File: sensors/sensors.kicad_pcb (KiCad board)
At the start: 2 copper layers, 75 x 56 mm, 29 parts, among them J1 GPIO, J2 PWM, J3 Conn_01x16, J5 JP_GPS, J6 JP_RADIO, U1 SC16IS752IPW, Y1 14.7456MHz

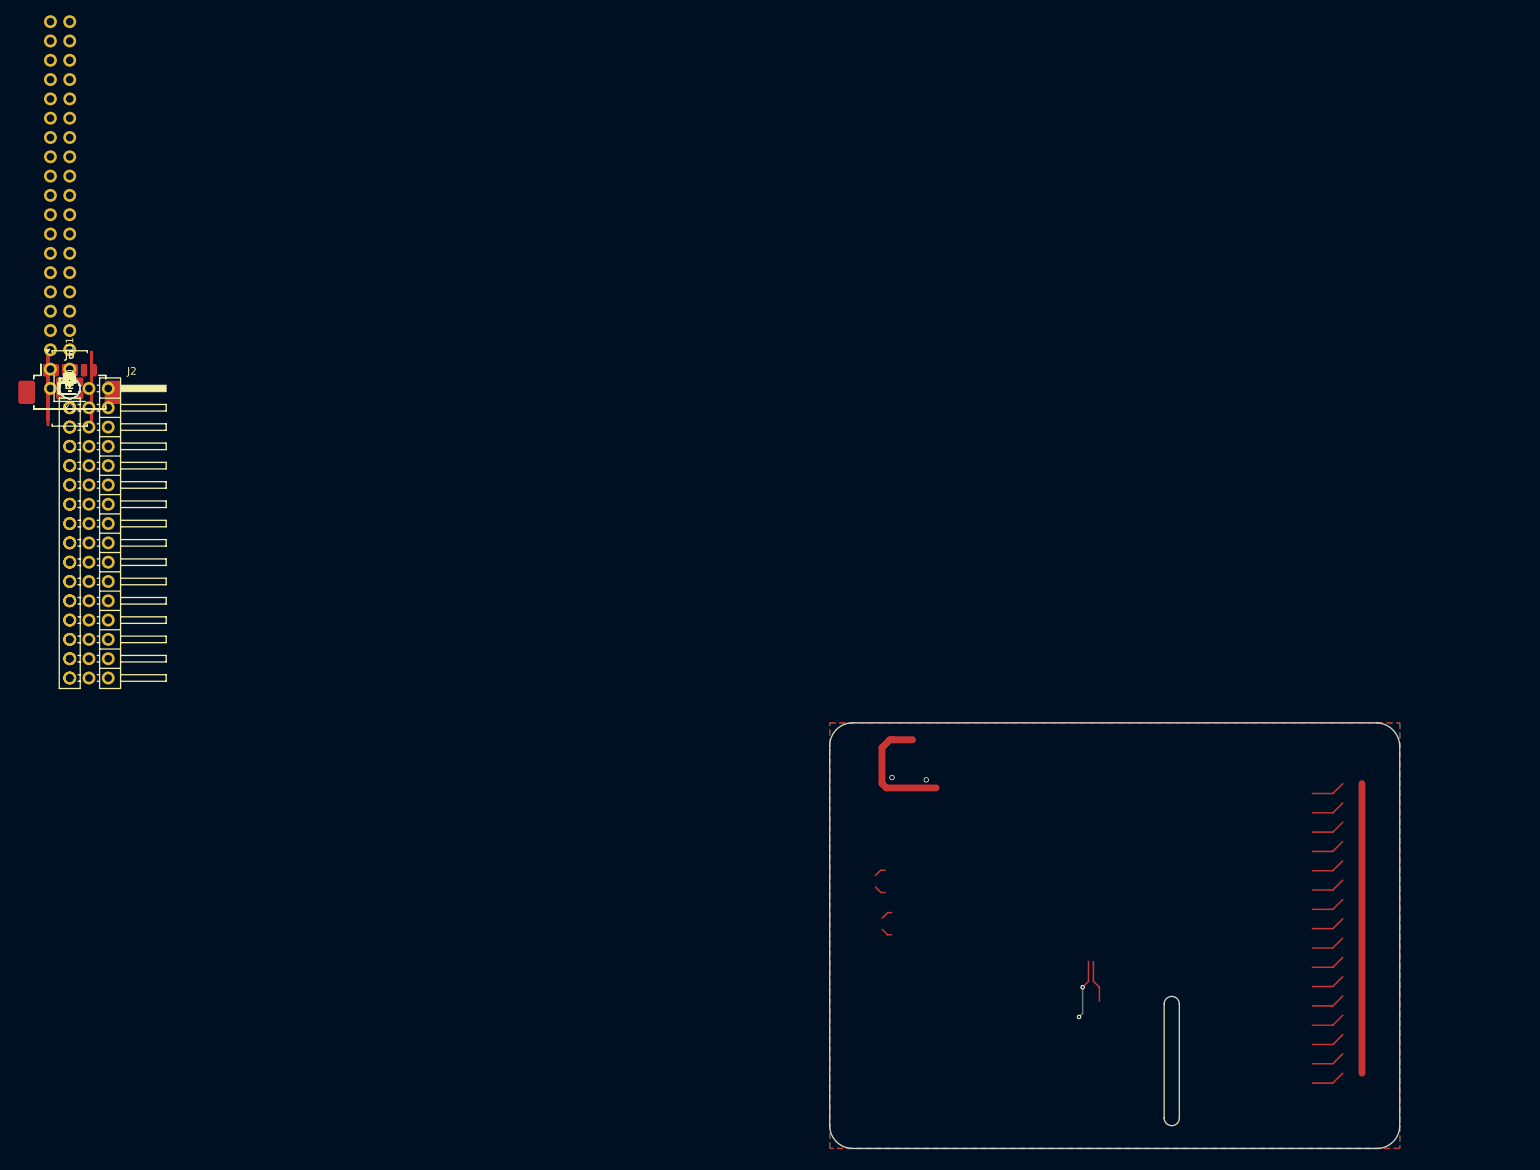
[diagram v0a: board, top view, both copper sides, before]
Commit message: add IMU
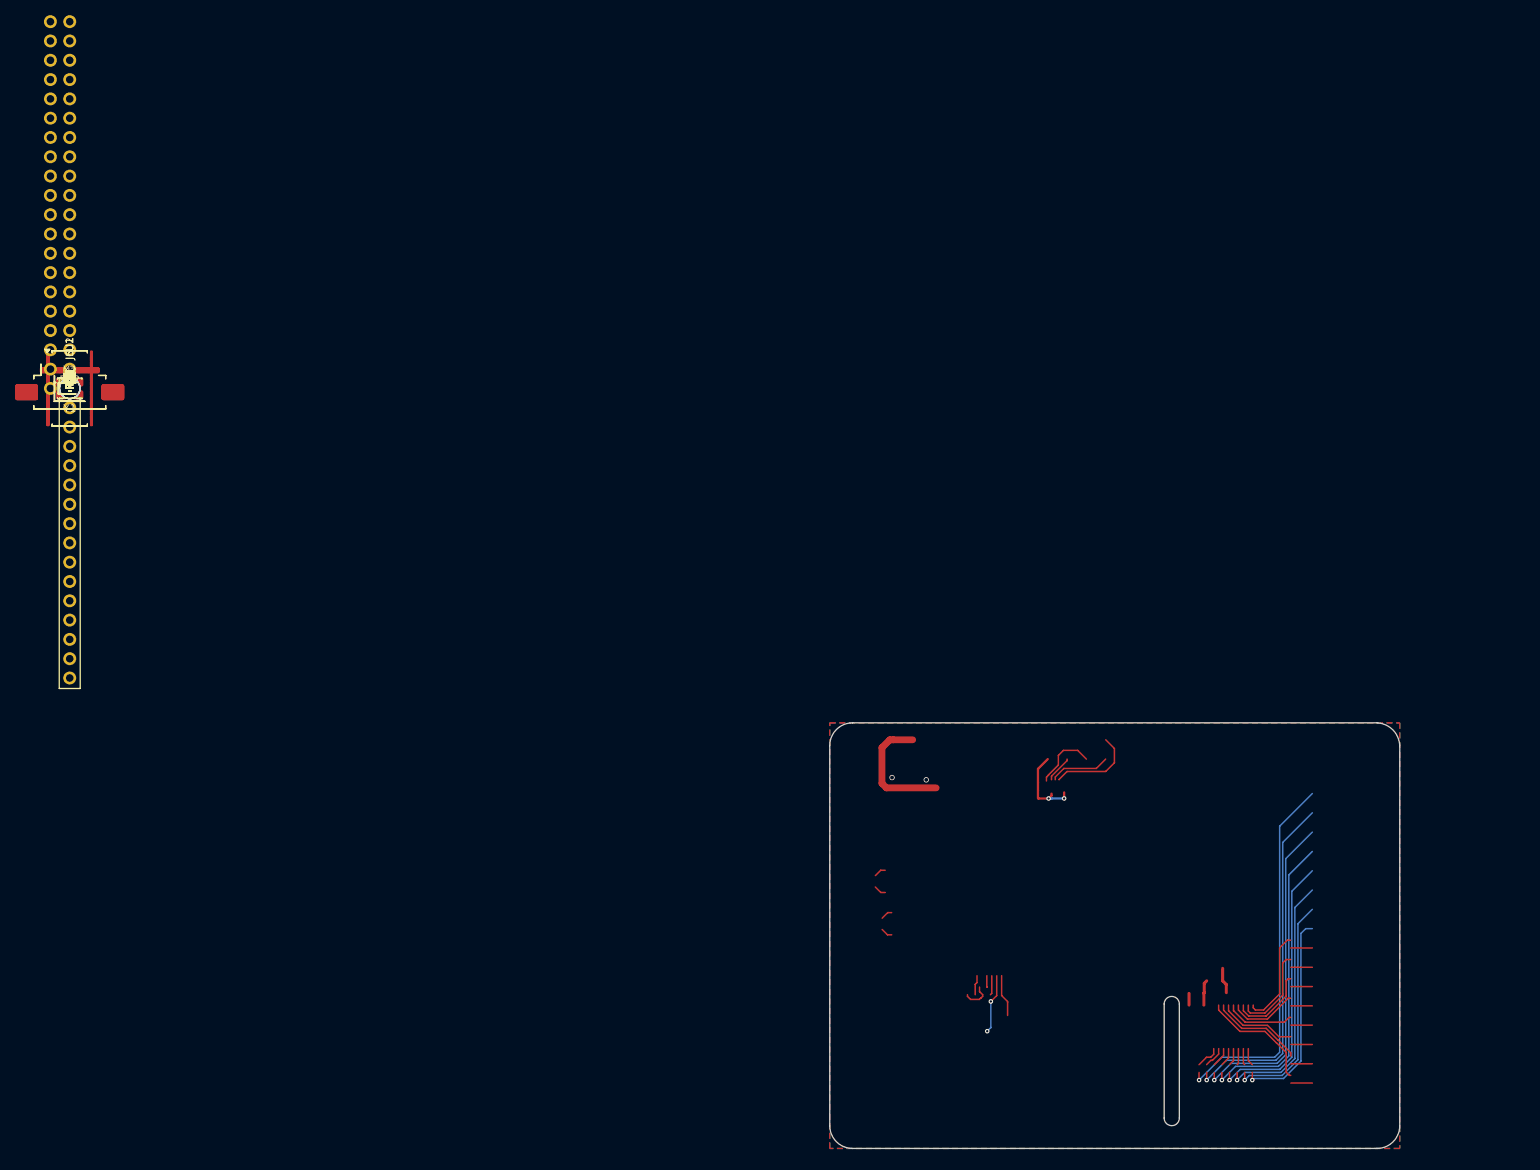
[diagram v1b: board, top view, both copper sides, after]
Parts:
- removed J2: PWM, pilotpi:PinHeader_3x16_P2.54mm_Horizontal
- added C4, C5, C6: 100nF (104) 10% 16V, Capacitor_SMD:C_0402_1005Metric, F.Cu at (0.00, 0.00)
- added C7: 220nF (224) 10% 16V, Capacitor_SMD:C_0402_1005Metric, F.Cu at (0.00, 0.00)
- added C8: 10nF (103) 10% 50V, Capacitor_SMD:C_0402_1005Metric, F.Cu at (0.00, 0.00)
- added R12: 3.3KΩ (3301) ±1%, Resistor_SMD:R_0402_1005Metric, F.Cu at (0.00, 0.00)
- added R13, R14, R15, R16, R17, R18, R19, R20, R21, R22, R23, R24, R25, R26, R27, R28: 220Ω (2200) ±1%, Resistor_SMD:R_0402_1005Metric, F.Cu at (0.00, 0.00)
- added U2: PCA9685PW, Package_SO:TSSOP-28_4.4x9.7mm_P0.65mm, F.Cu at (0.00, 0.00)
- added U3: ICM-42605, Package_LGA:LGA-14_3x2.5mm_P0.5mm_LayoutBorder3x4y, F.Cu at (0.00, 0.00)
- added Y2: ASE-xxxMHz, Oscillator:Oscillator_SMD_Abracon_ASE-4Pin_3.2x2.5mm, F.Cu at (0.00, 0.00)
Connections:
- J3 pad 1: /PWM15 -> /PWM0
- J3 pad 10: /PWM6 -> /PWM9
- J3 pad 11: /PWM5 -> /PWM10
- J3 pad 12: /PWM4 -> /PWM11
- J3 pad 13: /PWM3 -> /PWM12
- J3 pad 14: /PWM2 -> /PWM13
- J3 pad 15: /PWM1 -> /PWM14
- J3 pad 16: /PWM0 -> /PWM15
- J3 pad 2: /PWM14 -> /PWM1
- J3 pad 3: /PWM13 -> /PWM2
- J3 pad 4: /PWM12 -> /PWM3
- J3 pad 5: /PWM11 -> /PWM4
- J3 pad 6: /PWM10 -> /PWM5
- J3 pad 7: /PWM9 -> /PWM6
- J3 pad 8: /PWM8 -> /PWM7
- J3 pad 9: /PWM7 -> /PWM8
- J5 pad 4: unconnected-(J5-Pin_4-Pad4) -> /UART/CTSA
- J5 pad 5: unconnected-(J5-Pin_5-Pad5) -> /UART/RTSA
- R4 pad 1: GND -> +3V3
- R4 pad 2: Net-(U1-~{CTSA}) -> /UART/CTSA
- U1 pad 1: unconnected-(U1-~{RTSA}-Pad1) -> /UART/RTSA
- U1 pad 2: Net-(U1-~{CTSA}) -> /UART/CTSA
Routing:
- net /PWM0: track 4.54 -> 48.9 mm, vias 0 -> 1
- net /PWM1: track 4.54 -> 45.7 mm, vias 0 -> 1
- net /VCC_PWM: track 38.1 -> 0.00 mm
- net /PWM2: track 4.54 -> 42.5 mm, vias 0 -> 1
- net /PWM3: track 4.54 -> 39.3 mm, vias 0 -> 1
- net /PWM4: track 4.54 -> 36.1 mm, vias 0 -> 1
- net /PWM5: track 4.54 -> 32.9 mm, vias 0 -> 1
- net /PWM6: track 4.54 -> 29.7 mm, vias 0 -> 1
- net /PWM7: track 4.54 -> 27.0 mm, vias 0 -> 1
- net +3V3: track 0.00 -> 18.1 mm, vias 0 -> 2
- net Net-(U2-LED15): track 0.00 -> 15.2 mm
- net Net-(U2-LED8): track 0.00 -> 12.8 mm
- net Net-(U2-LED14): track 0.00 -> 12.3 mm
- net Net-(U2-LED9): track 0.00 -> 11.9 mm
- net /GPIO8/SPI0.CE0: track 0.00 -> 11.7 mm
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
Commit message: add magnetometer
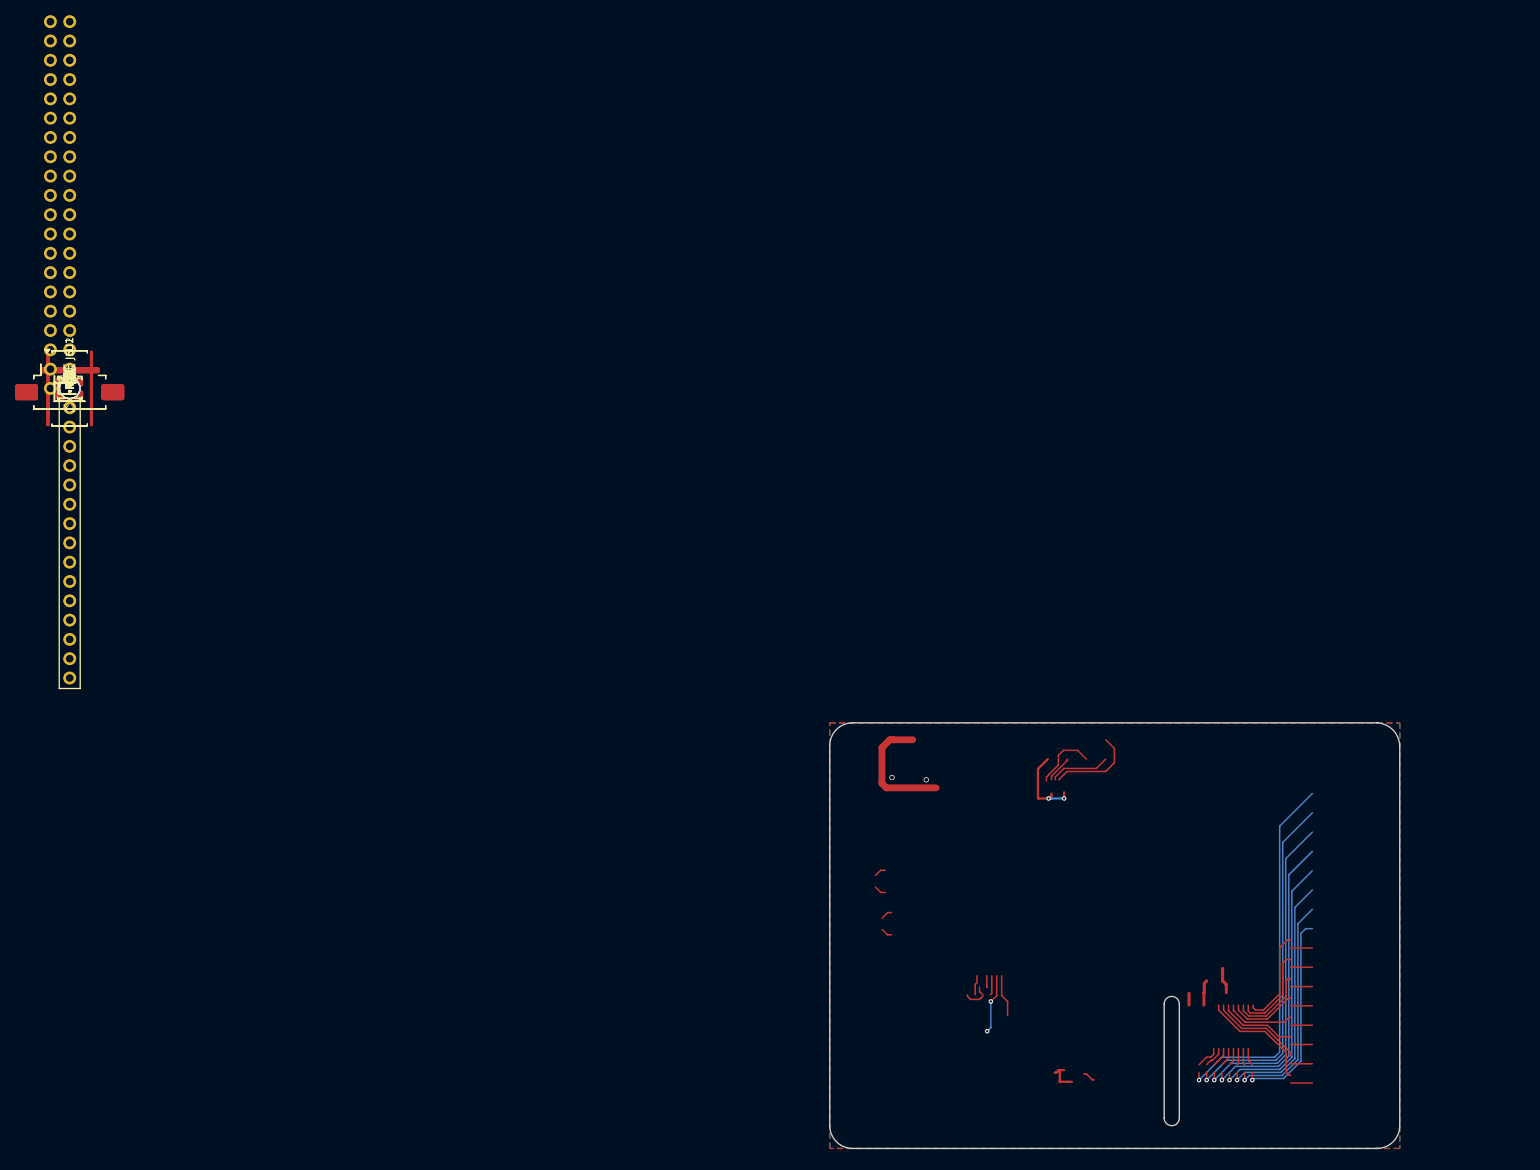
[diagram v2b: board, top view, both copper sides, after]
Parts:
- added C10: 470nF (474) 10% 25V, Capacitor_SMD:C_0603_1608Metric, F.Cu at (0.00, 0.00)
- added C9: 100nF (104) 10% 16V, Capacitor_SMD:C_0402_1005Metric, F.Cu at (0.00, 0.00)
- added U4: IST8310, Package_LGA:LGA-16_3x3mm_P0.5mm, F.Cu at (0.00, 0.00)
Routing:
- net +3V3: track 18.1 -> 22.6 mm
- net Net-(U4-C1): track 0.00 -> 1.72 mm

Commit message: add barometer & RC inverter
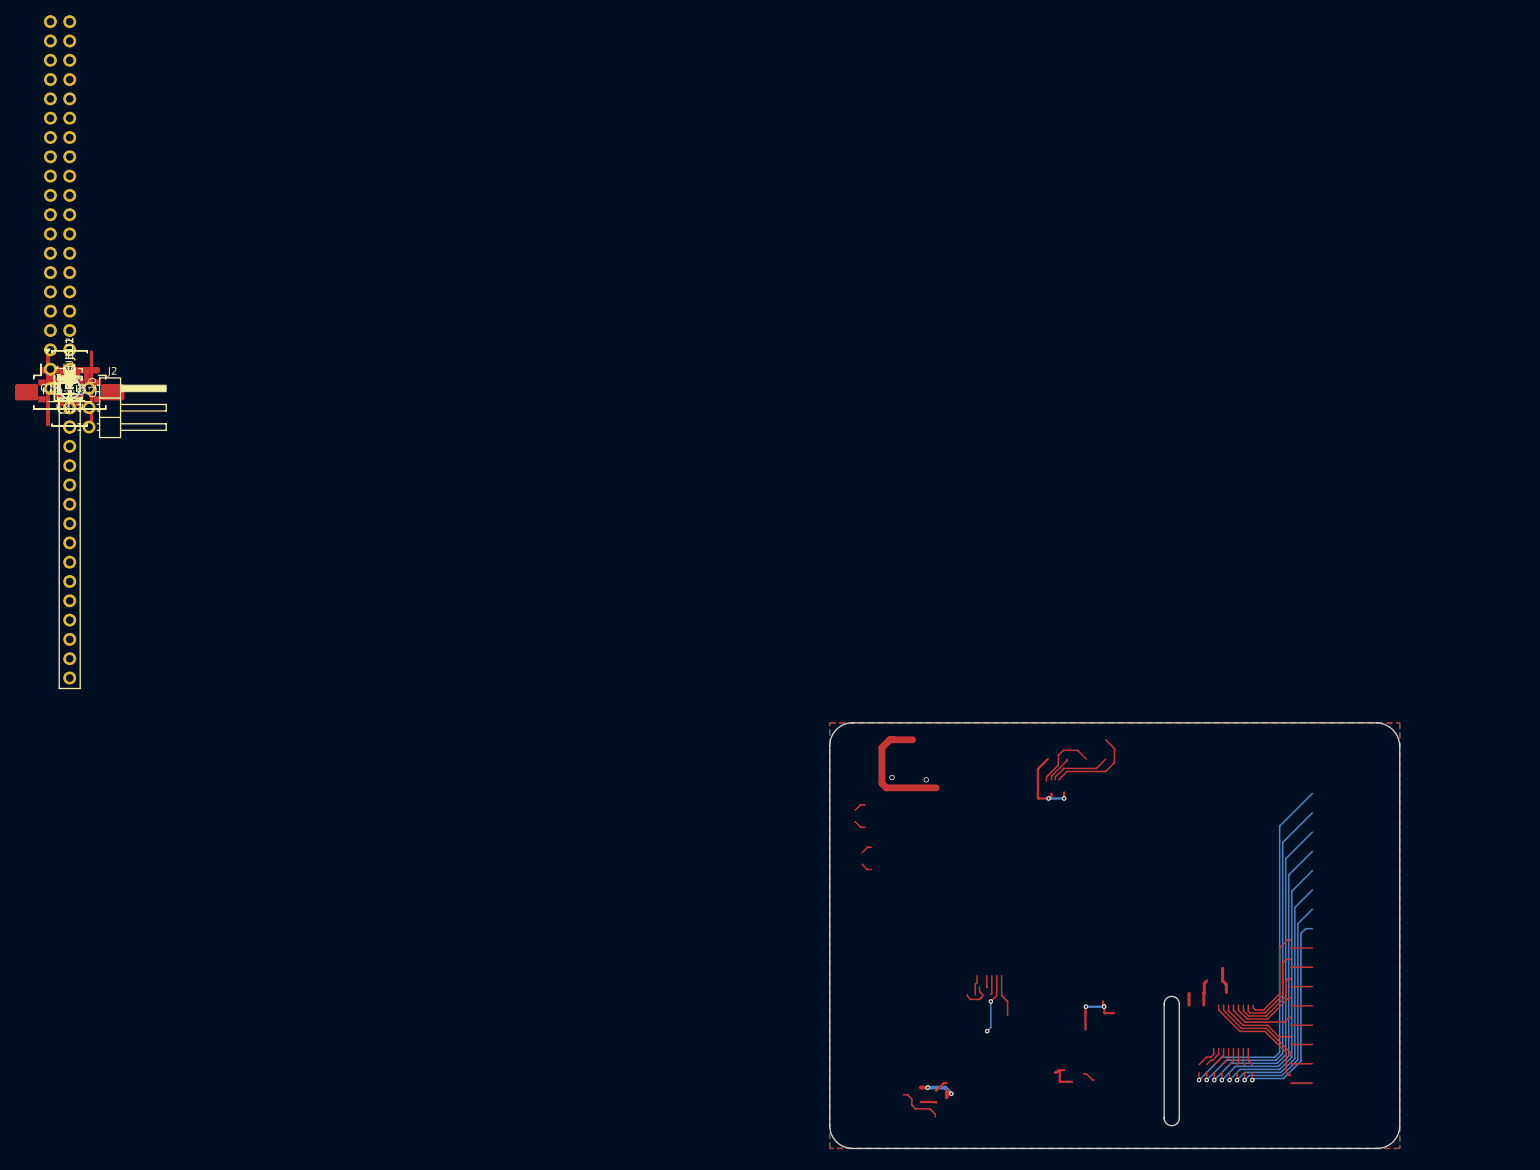
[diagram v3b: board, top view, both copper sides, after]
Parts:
- added C11: 100nF (104) 10% 16V, Capacitor_SMD:C_0402_1005Metric, F.Cu at (0.00, 0.00)
- added D5: TX_RED, LED_SMD:LED_0603_1608Metric, F.Cu at (0.00, 0.00)
- added J2: JP1115CH1&2, Connector_PinHeader_2.54mm:PinHeader_2x03_P2.54mm_Horizontal, F.Cu at (0.00, 0.00)
- added R29, R30: 10KΩ (1002) ±1%, Resistor_SMD:R_0402_1005Metric, F.Cu at (0.00, 0.00)
- added R31: 470Ω (4700) ±1%, Resistor_SMD:R_0402_1005Metric, F.Cu at (0.00, 0.00)
- added SW1: SW_SPDT_321, Button_Switch_SMD:SW_SPDT_PCM12, F.Cu at (0.00, 0.00)
- added U5: MS5611-01BA, Package_LGA:LGA-8_3x5mm_P1.25mm, F.Cu at (0.00, 0.00)
- added U6: 74LVC1G86, Package_TO_SOT_SMD:SOT-23-5, F.Cu at (0.00, 0.00)
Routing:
- net +3V3: track 22.6 -> 37.6 mm, vias 2 -> 6
- net Net-(SW1-B): track 0.00 -> 6.07 mm
- net /GPIO15/RXD0: track 0.00 -> 2.07 mm
- net Net-(D5-A): track 0.00 -> 1.82 mm

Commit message: add ADC
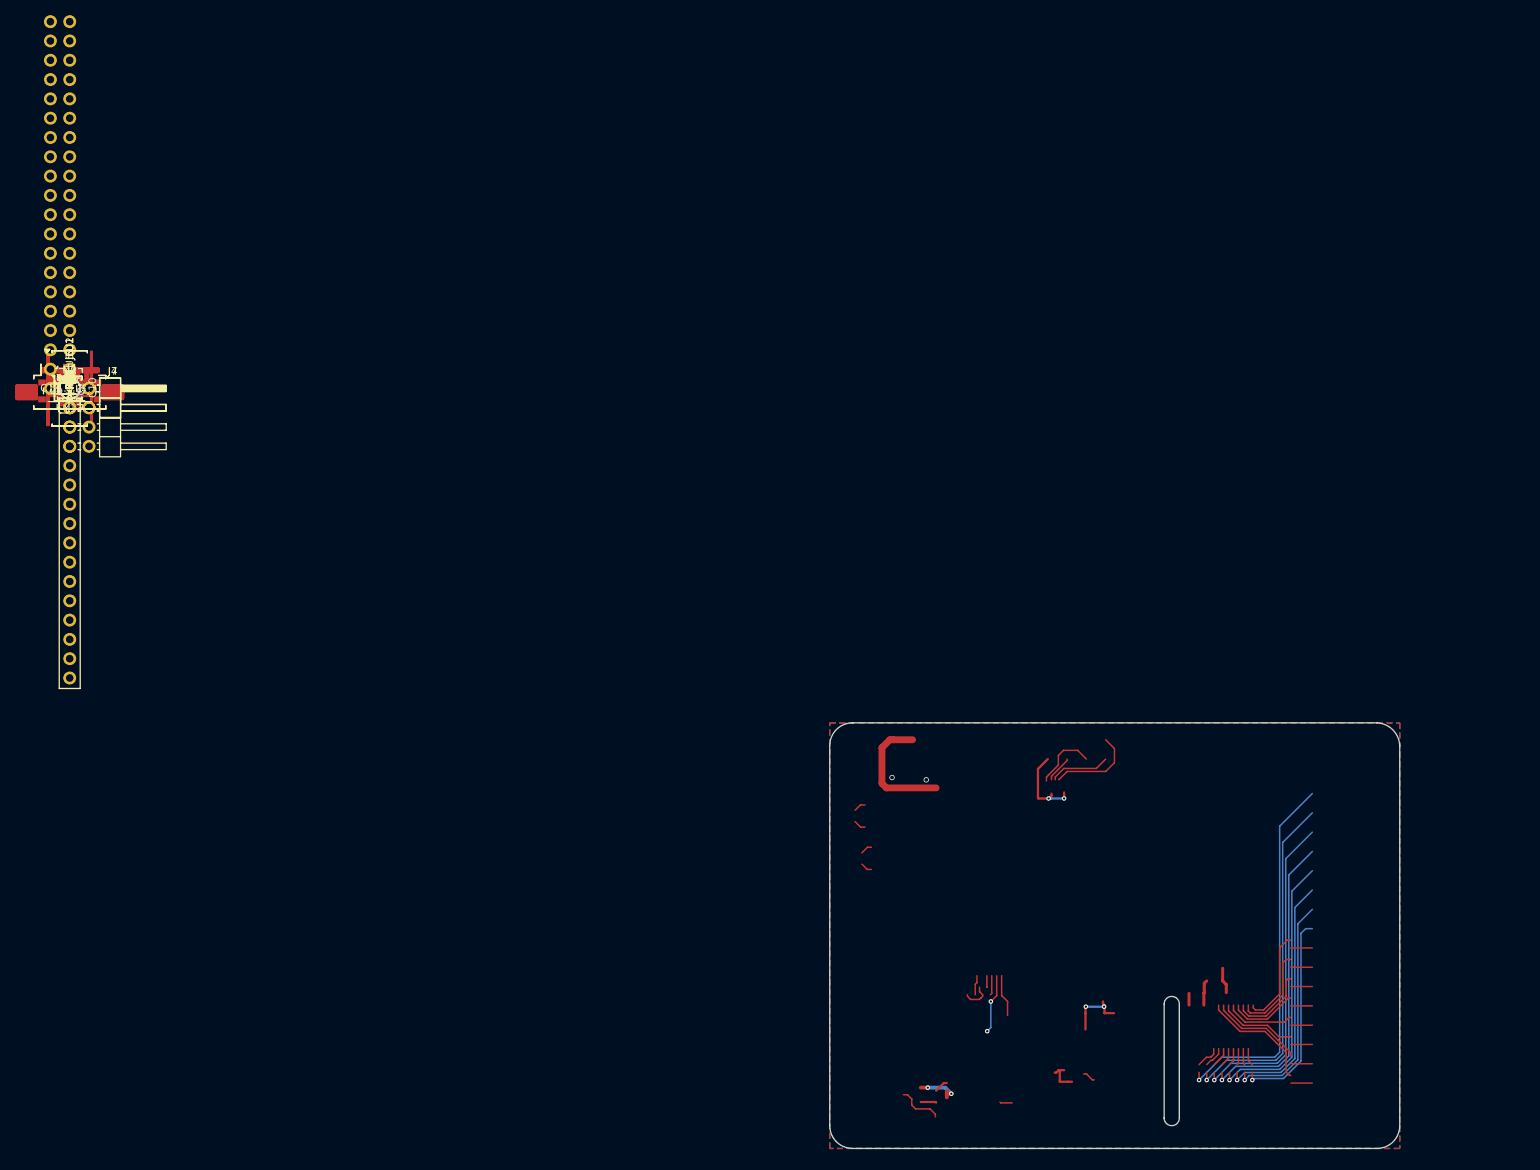
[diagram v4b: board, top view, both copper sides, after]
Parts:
- removed J2: JP1115CH1&2, Connector_PinHeader_2.54mm:PinHeader_2x03_P2.54mm_Horizontal
- added C12: 100nF (104) 10% 16V, Capacitor_SMD:C_0402_1005Metric, F.Cu at (0.00, 0.00)
- added J4: JP_ADC, Connector_PinHeader_2.54mm:PinHeader_2x04_P2.54mm_Horizontal, F.Cu at (0.00, 0.00)
- added J7: JP_RCIN, Connector_PinHeader_2.54mm:PinHeader_2x02_P2.54mm_Horizontal, F.Cu at (0.00, 0.00)
- added R32: 10KΩ (1002) ±1%, Resistor_SMD:R_0402_1005Metric, F.Cu at (0.00, 0.00)
- added U7: ADS1115IDGS, Package_SO:TSSOP-10_3x3mm_P0.5mm, F.Cu at (0.00, 0.00)
- J3: value Conn_01x16 -> JP_PWM
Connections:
- U6 pad 1: /SBUS/iBUS -> /RC inverter/RC
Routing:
- net Net-(U7-ADDR): track 0.00 -> 1.65 mm
